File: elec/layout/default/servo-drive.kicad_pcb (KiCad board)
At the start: 4 copper layers, 37.6 x 39.9 mm, 125 parts

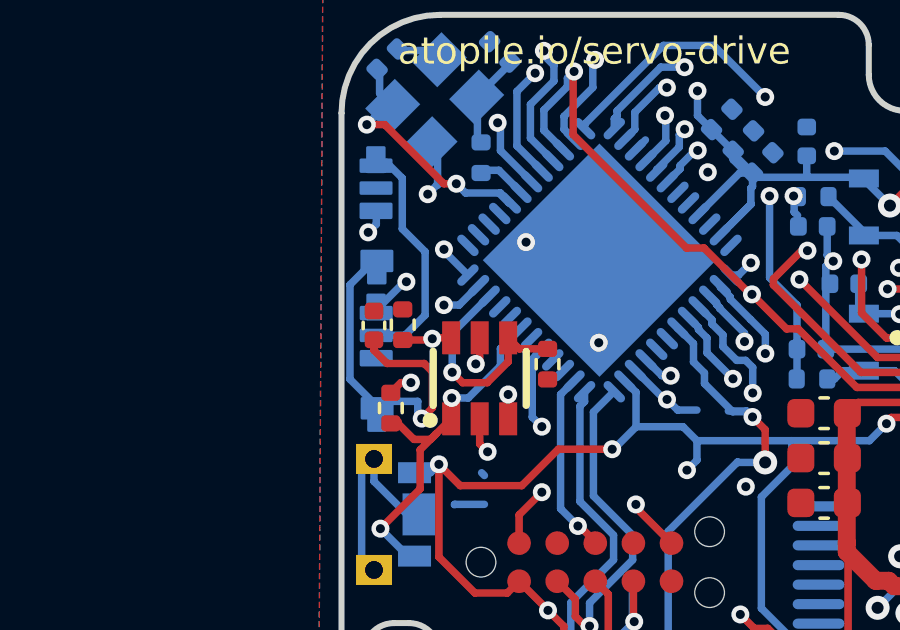
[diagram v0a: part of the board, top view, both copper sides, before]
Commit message: Update layout with pullup cap
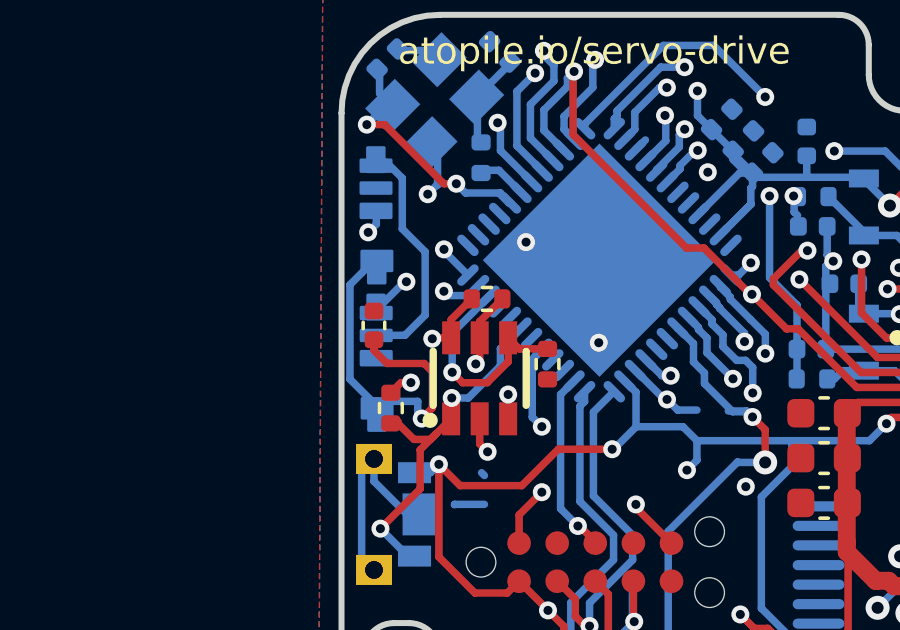
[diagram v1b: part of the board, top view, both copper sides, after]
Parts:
- C1: value 50V 1uF X5R ±10% 0603 Multilayer Ceramic Capacitors MLCC - SMD/SMT ROHS -> 10V 10uF X5R ±10% 0603 Multilayer Ceramic Capacitors MLCC - SMD/SMT ROHS
- C42, C44: value 50V 18pF C0G ±5% 0402 Multilayer Ceramic Capacitors MLCC - SMD/SMT ROHS -> 50V 22pF C0G ±5% 0402 Multilayer Ceramic Capacitors MLCC - SMD/SMT ROHS
- R10: value 62.5mW Thick Film Resistors 50V ±100ppm/℃ ±0.5% 27.4kΩ 0402 Chip Resistor - Surface Mount ROHS -> 62.5mW Thick Film Resistors 50V ±100ppm/℃ ±1% 27.4kΩ 0402 Chip Resistor - Surface Mount ROHS
- R16, R46, R52: value 62.5mW Thick Film Resistors 50V ±100ppm/℃ ±1% 73.2Ω 0402 Chip Resistor - Surface Mount ROHS -> 62.5mW Thick Film Resistors 50V -200ppm/℃~+500ppm/℃ ±1% 6.04Ω 0402 Chip Resistor - Surface Mount ROHS
- R18: value 62.5mW Thick Film Resistors 50V ±100ppm/℃ ±1% 6.34kΩ 0402 Chip Resistor - Surface Mount ROHS -> 62.5mW Thick Film Resistors 50V ±1% ±200ppm/℃ 6.34kΩ 0402 Chip Resistor - Surface Mount ROHS
- R31: value 62.5mW Thick Film Resistors 50V ±100ppm/℃ ±1% 41.2kΩ 0402 Chip Resistor - Surface Mount ROHS -> 62.5mW Thick Film Resistors 50V ±100ppm/℃ ±1% 43kΩ 0402 Chip Resistor - Surface Mount ROHS
- R4, R47, R8: value (none) -> 3mΩ +/- 1%
- R7: value 62.5mW Thick Film Resistors 50V ±100ppm/℃ ±1% 220Ω 0402 Chip Resistor - Surface Mount ROHS -> 62.5mW Thick Film Resistors 50V ±100ppm/℃ ±1% 200Ω 0402 Chip Resistor - Surface Mount ROHS
- moved R3 2.94 mm to (209.8, 91.2), turned to 0 degrees
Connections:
- net power_stage.phase_a.current_sensor.bias_div-vcc renamed power_stage.phase_a.current_sensor.net_tie_p-_shunt_p
- net power_stage.phase_a.current_sensor.feedback_div-vcc renamed power_stage.phase_a.current_sensor.net_tie_n-_shunt_n
- net power_stage.phase_a.half_bridge-vcc-2 renamed power_stage.phase_a.half_bridge-io
- net power_stage.phase_b.current_sensor.bias_div-vcc renamed power_stage.phase_b.current_sensor.net_tie_p-_shunt_p
- net power_stage.phase_b.current_sensor.feedback_div-vcc renamed power_stage.phase_b.current_sensor.net_tie_n-_shunt_n
- net power_stage.phase_b.half_bridge-vcc-2 renamed power_stage.phase_b.half_bridge-io
- net power_stage.phase_c.current_sensor.bias_div-vcc renamed power_stage.phase_c.current_sensor.net_tie_p-_shunt_p
- net power_stage.phase_c.current_sensor.feedback_div-vcc renamed power_stage.phase_c.current_sensor.net_tie_n-_shunt_n
- net power_stage.phase_c.half_bridge-vcc-2 renamed power_stage.phase_c.half_bridge-io
- R3 pad 2: power_stage-gnd -> power_stage-vcc-2
- U13 pad 20: (no net) -> power_stage-vcc-2
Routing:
- net power_stage-vcc-2: track 108.8 -> 110.4 mm
- net micro.micro-io-1: track 16.4 -> 17.0 mm

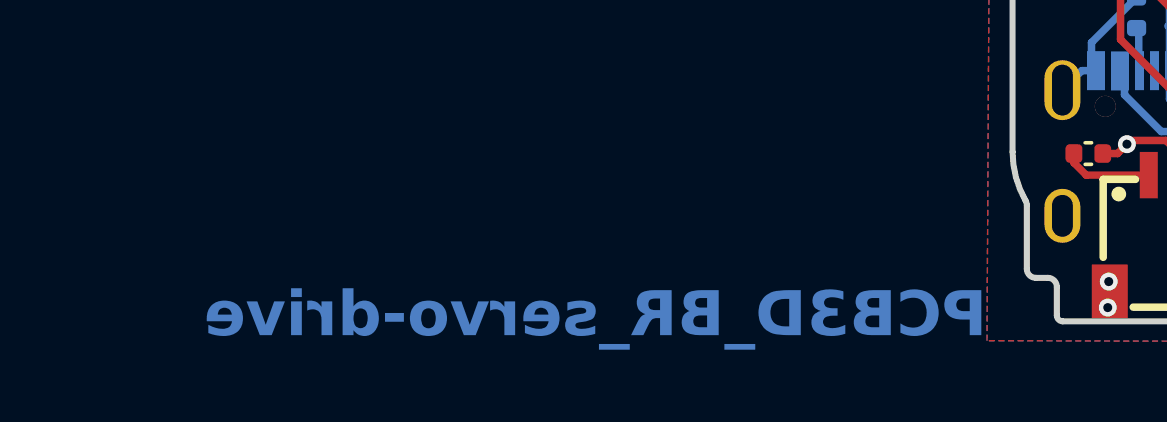
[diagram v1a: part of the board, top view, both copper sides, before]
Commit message: manually override bad net names
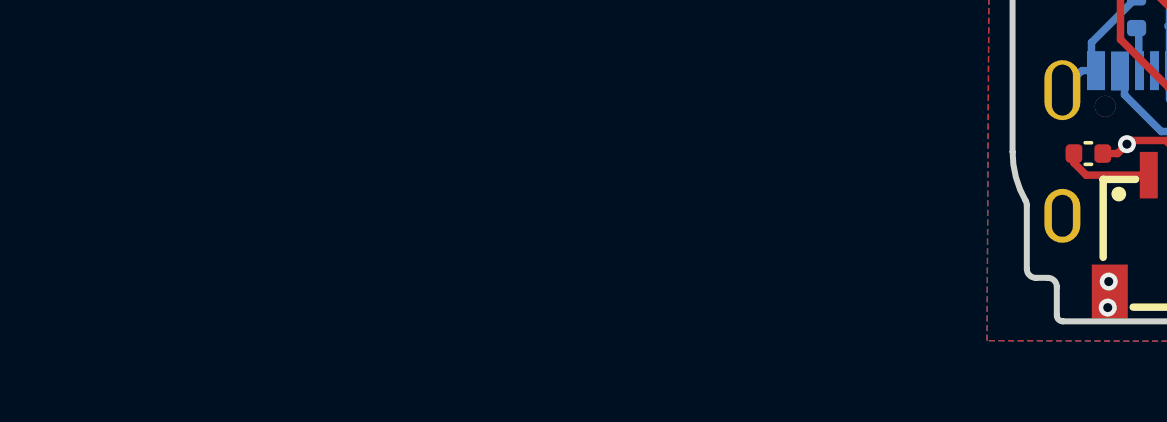
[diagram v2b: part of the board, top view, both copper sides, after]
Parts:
- C12: renamed from C29; value (none) -> ?
- C13: renamed from C22; value (none) -> ?
- C14: renamed from C6; value (none) -> ?
- C15: renamed from C27; value (none) -> ?
- C16: renamed from C26; value (none) -> ?
- C17: renamed from C4; value (none) -> ?
- C18: renamed from C3; value (none) -> ?
- C19: renamed from C25; value (none) -> ?
- C20: renamed from C21; value (none) -> ?
- C21: renamed from C20; value (none) -> ?
- C22: renamed from C30; value (none) -> ?
- C23: renamed from C35; value (none) -> ?
- C24: renamed from C36; value (none) -> ?
- C25: renamed from C37; value (none) -> ?
- C26: renamed from C38; value (none) -> ?
- C27: renamed from C47; value (none) -> ?
- C28: renamed from C48; value (none) -> ?
- C29: renamed from C49; value (none) -> ?
- C30: renamed from C39; value (none) -> ?
- C43: renamed from C42; value 50V 22pF C0G ±5% 0402 Multilayer Ceramic Capacitors MLCC - SMD/SMT ROHS -> 50V 20pF C0G ±5% 0402 Multilayer Ceramic Capacitors MLCC - SMD/SMT ROHS
- C44: value 50V 22pF C0G ±5% 0402 Multilayer Ceramic Capacitors MLCC - SMD/SMT ROHS -> 50V 20pF C0G ±5% 0402 Multilayer Ceramic Capacitors MLCC - SMD/SMT ROHS
- DS1: renamed from U36; value (none) -> ?
- DS2: renamed from U30; value (none) -> ?
- J1: renamed from U14; value (none) -> ?
- J2: renamed from U2; value (none) -> ?
- J3: renamed from U15; value (none) -> ?
- J4: renamed from U26; value (none) -> ?
- J5: renamed from U27; value (none) -> ?
- L1: renamed from U10; value (none) -> ?
- R1: renamed from R4; value 3mΩ +/- 1% -> ?
- R13: renamed from R47; value 3mΩ +/- 1% -> ?
- R19: renamed from R31; value 62.5mW Thick Film Resistors 50V ±100ppm/℃ ±1% 43kΩ 0402 Chip Resistor - Surface Mount ROHS -> 62.5mW Thick Film Resistors 50V ±100ppm/℃ ±1% 39kΩ 0402 Chip Resistor - Surface Mount ROHS
- R25: renamed from R18; value 62.5mW Thick Film Resistors 50V ±1% ±200ppm/℃ 6.34kΩ 0402 Chip Resistor - Surface Mount ROHS -> 62.5mW Thick Film Resistors 50V ±100ppm/℃ ±1% 6.34kΩ 0402 Chip Resistor - Surface Mount ROHS
- R27: renamed from R22; value 62.5mW Thick Film Resistors 50V ±100ppm/℃ ±1% 6.2kΩ 0402 Chip Resistor - Surface Mount ROHS -> 62.5mW Thick Film Resistors 50V ±100ppm/℃ ±1% 6.19kΩ 0402 Chip Resistor - Surface Mount ROHS
- R36: renamed from R19; value 10kohm +/- 1% -> ?
- R7: renamed from R8; value 3mΩ +/- 1% -> ?
- U1: renamed from U28; value (none) -> ?
- U10: renamed from U34; value (none) -> ?
- U11: renamed from U35; value (none) -> ?
- U12: renamed from U24; value (none) -> ?
- U13: renamed from U12; value (none) -> ?
- U14: renamed from U4; value (none) -> ?
- U15: renamed from U6; value (none) -> 0.6A, 42V, 1.1MHz Buck Regulator
- U16: renamed from U22; value (none) -> ?
- U17: renamed from U23; value (none) -> ?
- U18: renamed from U13; value (none) -> ?
- U19: renamed from U37; value (none) -> ?
- U2: renamed from U17; value (none) -> ?
- U20: renamed from U25; value (none) -> ?
- U21: renamed from U18; value (none) -> 15Ω 1 SPDT(SPDT) SOT-23-6 Analog Switches / Multiplexers ROHS
- U22: renamed from U16; value (none) -> ?
- U23: renamed from U29; value (none) -> ?
- U24: renamed from J1; value (none) -> ?
- U25: renamed from U7; value (none) -> ?
- U26: renamed from U8; value (none) -> ?
- U27: renamed from U9; value (none) -> ?
- U28: renamed from U5; value (none) -> ?
- U29: renamed from U32; value (none) -> ?
- U3: renamed from U19; value (none) -> ?
- U30: renamed from U11; value (none) -> ?
- U4: renamed from U20; value (none) -> ?
- U5: renamed from U1; value (none) -> ?
- U6: renamed from U31; value (none) -> ?
- U7: renamed from U33; value (none) -> ?
- U8: renamed from U21; value (none) -> ?
- U9: renamed from U3; value (none) -> ?
- renumbered C10 to C1, C2 to C10, C7 to C11, C11 to C2, C12 to C3, C1 to C31, C8 to C32, C24 to C33, C5 to C34, C9 to C35, C14 to C36, C15 to C37, C17 to C38, C40 to C39, C32 to C4, C13 to C40, C51 to C41, C50 to C42, C16 to C45, C18 to C46, C19 to C47, C28 to C48, C33 to C49, C23 to C5, C34 to C50, C31 to C6, C41 to C7, C43 to C8, C45 to C9, R44 to R10, R45 to R11, R46 to R12, R48 to R14, R49 to R15, R50 to R16, R51 to R17, R52 to R18, R6 to R2, R1 to R20, R38 to R21, R29 to R22, R30 to R23, R17 to R24, R21 to R26, R2 to R28, R7 to R29, R12 to R3, R3 to R30, R5 to R31, R9 to R32, R10 to R33, R11 to R34, R15 to R35, R20 to R37, R13 to R4, R14 to R5, R16 to R6, R25 to R8, R26 to R9
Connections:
- net canh renamed CANH
- net canl renamed CANL
- net dm renamed DM_USB
- net dp renamed DP_USB
- net micro-miso renamed MISO_SPI
- net micro-mosi renamed MOSI_SPI
- net micro-sda renamed SDA_I2C
- net micro.micro-miso renamed miso
- net micro.micro-mosi renamed mosi
- net micro.micro-sda renamed sda
- net power_stage-gnd renamed GND
- net power_stage-vcc renamed VCC_BATT
- net power_stage-vcc-1 renamed VCC_GATE
- net power_stage-vcc-2 renamed VCC_3V3
- net power_stage.phase_a.half_bridge-io renamed OUT_A
- net power_stage.phase_b.half_bridge-io renamed OUT_B
- net power_stage.phase_c.half_bridge-io renamed OUT_C
- net power_supply-vcc-1 renamed VCC_5V
- net rx renamed CAN_RX
- net sck renamed SCK_SPI
- net scl renamed SCL_I2C
- net tx renamed CAN_TX
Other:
- board text removed: "PCB3D_BR_servo-drive"
- board text removed: "PCB3D_TL_servo-drive"

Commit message: fix naming
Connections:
- net micro-vcc-2 renamed TEMP_SENSE
- net micro-vcc-3 renamed BATT_SENSE
- net power_supply-vcc renamed VCC_USB
- C1 pad 1: power_stage.phase_a.current_sensor-vcc-1 -> power_stage.phase_a.current_sensor-vcc
- R11 pad 2: power_stage.phase_a.current_sensor-vcc -> VCC_VREF
- R17 pad 2: power_stage.phase_a.current_sensor-vcc -> VCC_VREF
- R37 pad 2: micro-vcc-1 -> micro-vcc
- R5 pad 2: power_stage.phase_a.current_sensor-vcc -> VCC_VREF
- R6 pad 2: power_stage.phase_a.current_sensor-vcc-1 -> power_stage.phase_a.current_sensor-vcc
- U14 pad 3: power_stage.phase_a.current_sensor-vcc -> VCC_VREF
- U14 pad 4: power_stage.phase_a.current_sensor-vcc -> VCC_VREF
- U18 pad 17: power_stage.phase_a.current_sensor-vcc-1 -> power_stage.phase_a.current_sensor-vcc
- U18 pad 29: micro-vcc -> LED_DATA
- U18 pad 32: micro-vcc-4 -> micro-vcc-1
- U18 pad 43: micro-vcc-1 -> micro-vcc
- U21 pad 1: micro-vcc-1 -> micro-vcc
- U28 pad 4: micro-vcc -> LED_DATA
- U30 pad 1: micro-vcc-1 -> micro-vcc
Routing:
- net VCC_VREF: track 0.00 -> 47.6 mm, vias 0 -> 5
- net power_stage.phase_a.current_sensor-vcc: track 47.6 -> 7.49 mm, vias 5 -> 2
- net LED_DATA: track 0.00 -> 25.6 mm, vias 0 -> 2
- net micro-vcc-1: track 13.3 -> 0.00 mm, vias 2 -> 0
- net micro-vcc: track 25.6 -> 13.3 mm
- net power_stage.phase_a.current_sensor-vcc-1: track 7.49 -> 0.00 mm, vias 2 -> 0
